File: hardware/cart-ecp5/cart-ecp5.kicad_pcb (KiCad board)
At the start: 4 copper layers, 100 x 60 mm, 139 parts, among them J1 JTAG, J2 MicroSD_Molex_1040310811, J3 N64_Cartridge_Bus, J5 USB_C_USB2.0, U1 LFE5U-25F-xBG256x, U10 93C46BT-I_OT, U11 FT2232HQ, U13 TLV62568DBV, U2 W25Q512JVEIM, U3 S27KS0641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

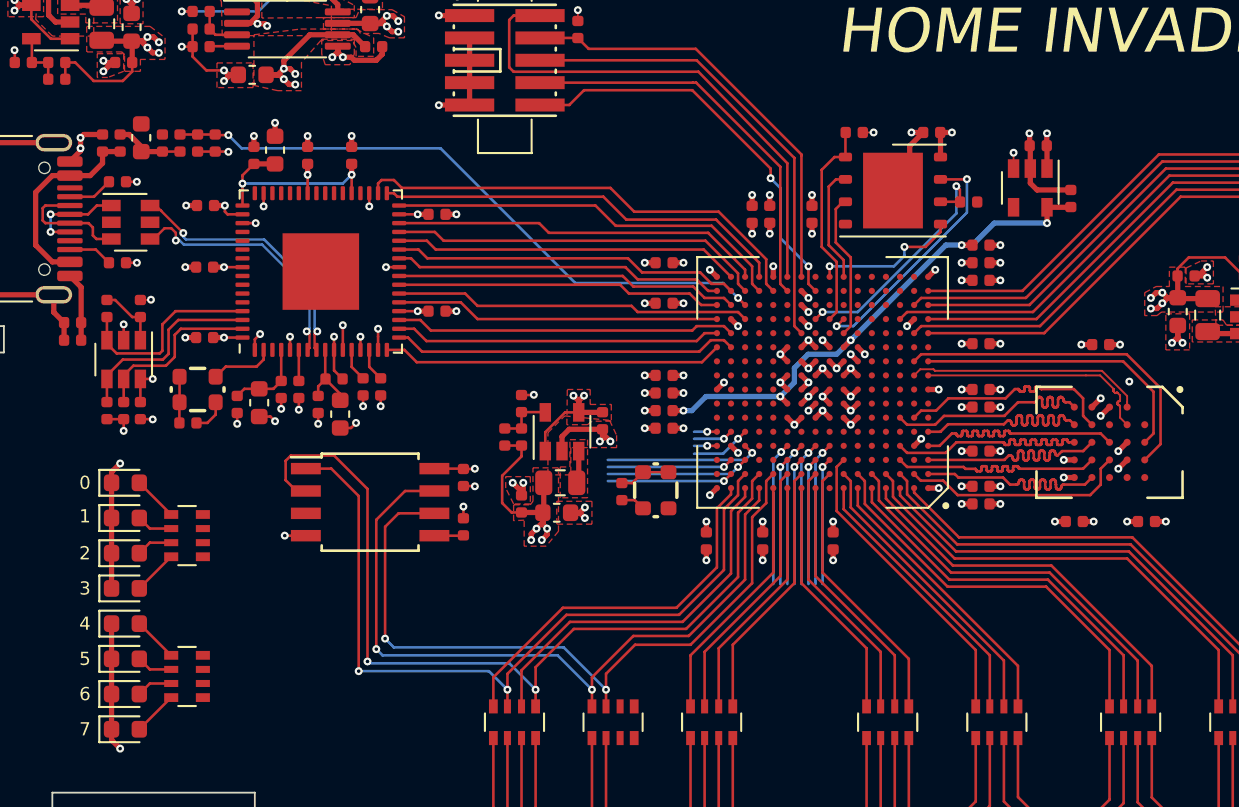
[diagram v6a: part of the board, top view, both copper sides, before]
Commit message: Assign FPGA IO for debugging LEDs and route signals
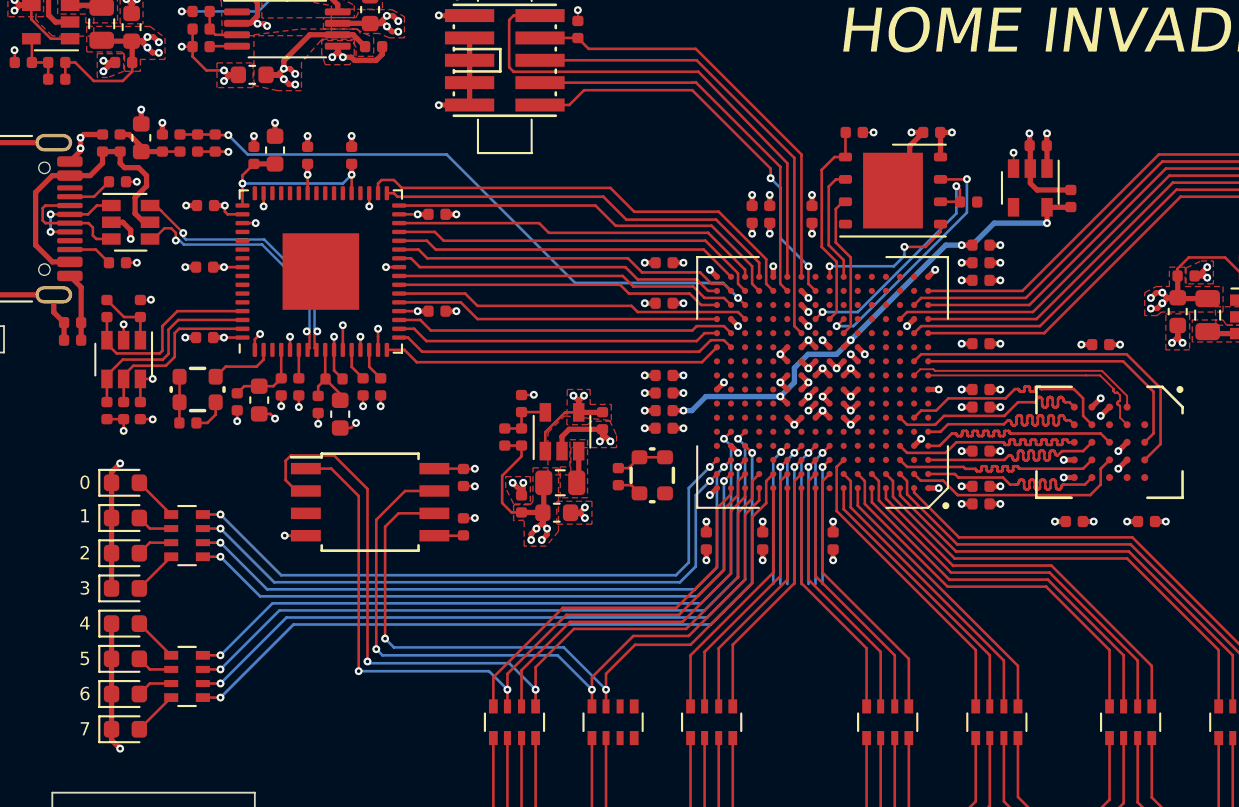
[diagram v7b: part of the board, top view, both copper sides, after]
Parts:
- moved X1 0.87 mm to (140.3, 105.5)
- moved C2 0.87 mm to (138.4, 105.5)
- moved FB1 0.15 mm to (116.8, 101.3)
- moved C21 0.15 mm to (118.0, 101.2)
- moved C23 0.15 mm to (119.2, 100.5)
- moved R22 0.15 mm to (120.2, 100.5)
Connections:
- U1 pad B15: Net-(U1-PadB15) -> LED_D3
- U1 pad B16: Net-(U1-PadB16) -> LED_D1
- U1 pad C14: Net-(U1-PadC14) -> LED_D5
- U1 pad C15: Net-(U1-PadC15) -> LED_D2
- U1 pad C16: Net-(U1-PadC16) -> LED_D0
- U1 pad D14: Net-(U1-PadD14) -> LED_D7
- U1 pad E14: Net-(U1-PadE14) -> LED_D6
- U1 pad E15: Net-(U1-PadE15) -> LED_D4
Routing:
- net LED_D6: track 0.00 -> 42.0 mm, vias 0 -> 2
- net LED_D7: track 0.00 -> 41.9 mm, vias 0 -> 2
- net LED_D4: track 0.00 -> 40.3 mm, vias 0 -> 2
- net LED_D5: track 0.00 -> 39.4 mm, vias 0 -> 2
- net LED_D2: track 0.00 -> 37.2 mm, vias 0 -> 2
- net LED_D3: track 0.00 -> 36.8 mm, vias 0 -> 2
- net LED_D0: track 0.00 -> 35.8 mm, vias 0 -> 2
- net LED_D1: track 0.00 -> 35.4 mm, vias 0 -> 2
- net Net-(U1-PadD14): track 8.93 -> 0.00 mm, vias 1 -> 0
- net Net-(U1-PadC14): track 8.13 -> 0.00 mm, vias 1 -> 0
- net Net-(U1-PadC15): track 7.17 -> 0.00 mm, vias 1 -> 0
- net Net-(U1-PadB15): track 7.17 -> 0.00 mm, vias 1 -> 0
- net /Interface-USB/USB_VBUS: track 11.5 -> 17.4 mm
- net Net-(U1-PadE14): track 3.42 -> 0.00 mm, vias 1 -> 0
- net GND: track 216.9 -> 220.2 mm, vias 128 -> 130
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
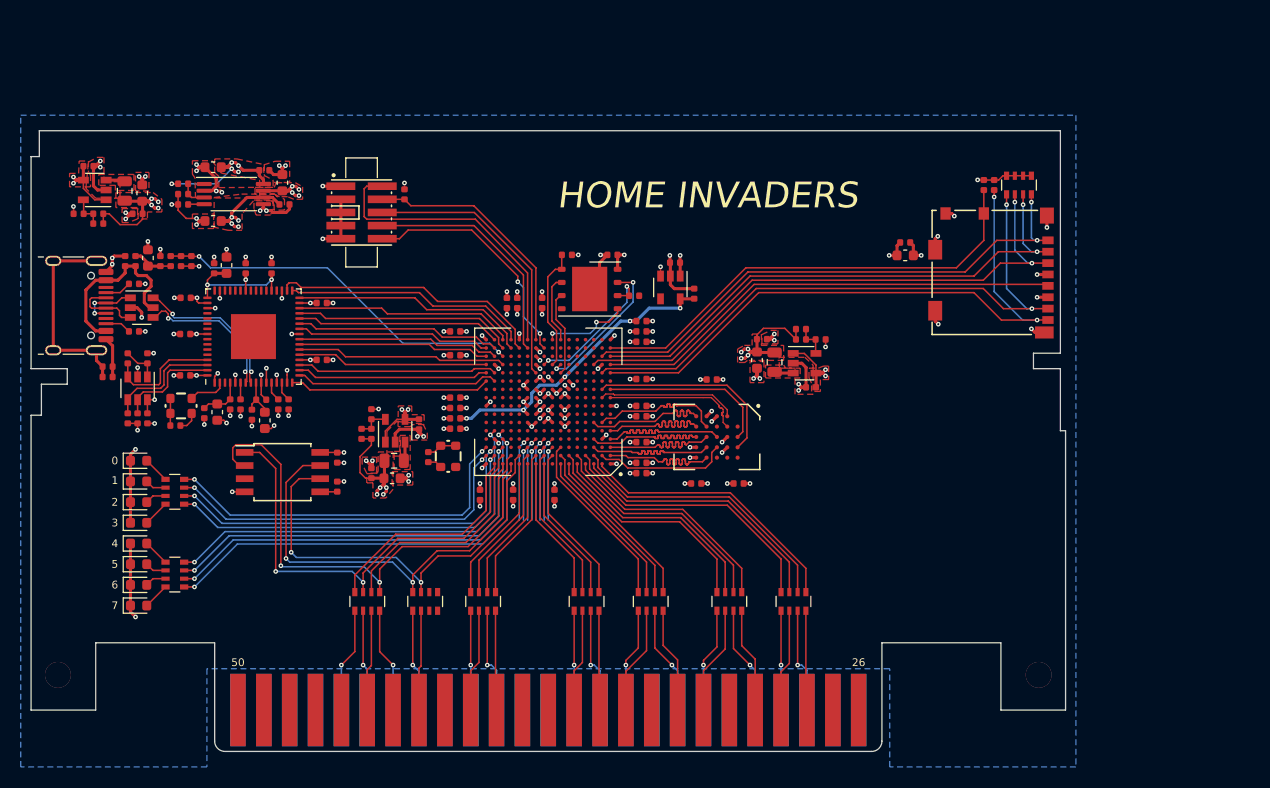
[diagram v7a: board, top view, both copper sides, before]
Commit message: Move MicroSD connector to top edge to make room for passthrough connectors
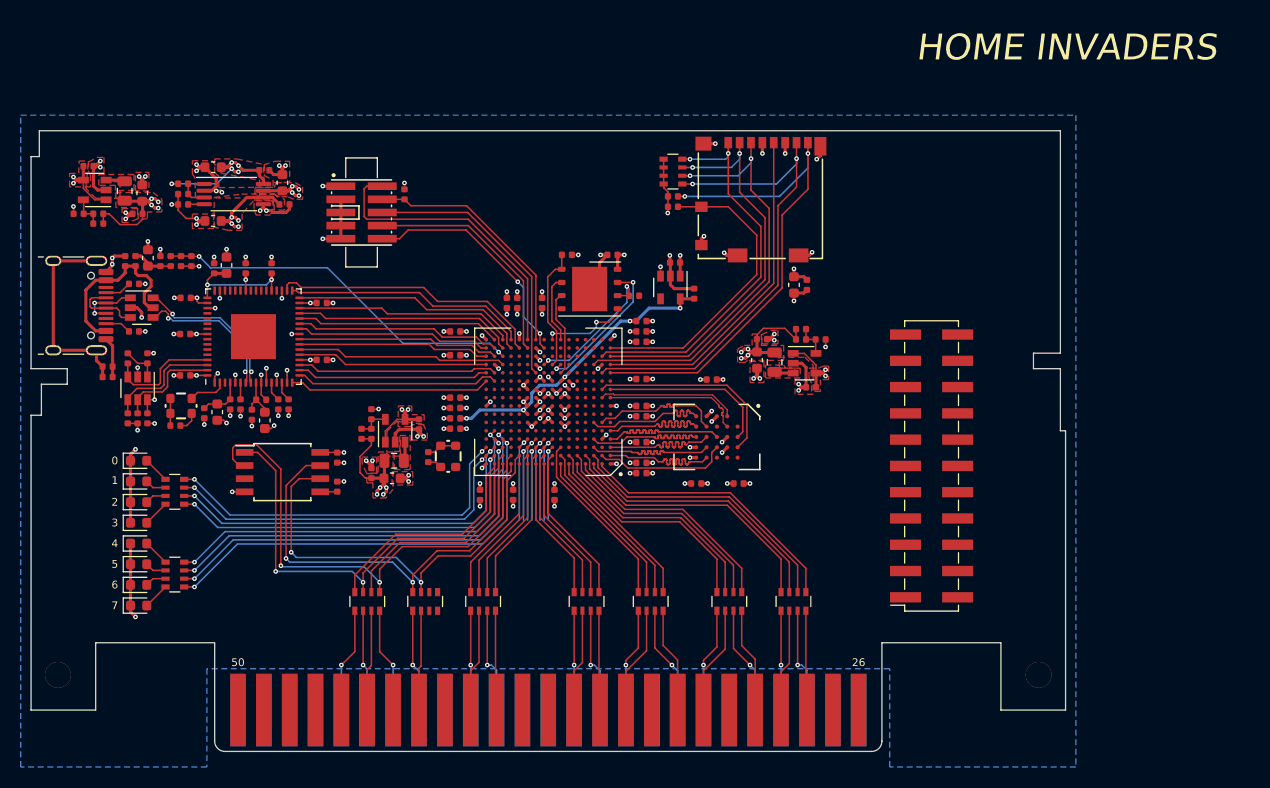
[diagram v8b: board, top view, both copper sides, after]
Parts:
- added REF**: PinSocket_2x11_P2.54mm_Vertical_SMD, Connector_PinSocket_2.54mm:PinSocket_2x11_P2.54mm_Vertical_SMD, F.Cu at (187.1, 106.4)
- moved RN7 33.5 mm to (162.1, 78.0), turned to 180 degrees
- moved R5 31.1 mm to (162.1, 80.3), turned to 0 degrees
- moved J2 30.5 mm to (170.5, 75.2), turned to 180 degrees
- moved R4 30.1 mm to (162.1, 81.3), turned to 0 degrees
- moved C3 11.1 mm to (173.8, 88.9), turned to 90 degrees
- moved C4 10.3 mm to (175.0, 88.9), turned to 90 degrees
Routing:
- net SD_CD: track 45.3 -> 29.6 mm
- net SD_DAT2: track 52.6 -> 37.7 mm
- net SD_DAT3: track 52.9 -> 38.7 mm
- net SD_CMD: track 55.5 -> 42.0 mm
- net SD_CLK: track 45.6 -> 32.9 mm
- net SD_DAT0: track 59.6 -> 47.4 mm
- net SD_DAT1: track 61.7 -> 50.2 mm
